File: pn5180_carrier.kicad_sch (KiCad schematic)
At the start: 35 parts, among them J1 Bay 0 (CLIK-Mate 1x10), J10 24V IN (CLIK-Mate 1x2), J2 Bay 1 (CLIK-Mate 1x10), J3 Bay 2 (CLIK-Mate 1x10), J4 Bay 3 (CLIK-Mate 1x10), J5 Bay 4 (CLIK-Mate 1x10), J6 Bay 5 (CLIK-Mate 1x10), J7 Bay 6 (CLIK-Mate 1x10), J8 Bay 7 (CLIK-Mate 1x10), U1 74HC138, U2 74HC151, U4 TLV1117LV33DCYR, U5 XIAO ESP32C6, U6 MP1584EN module (set 5.0V)

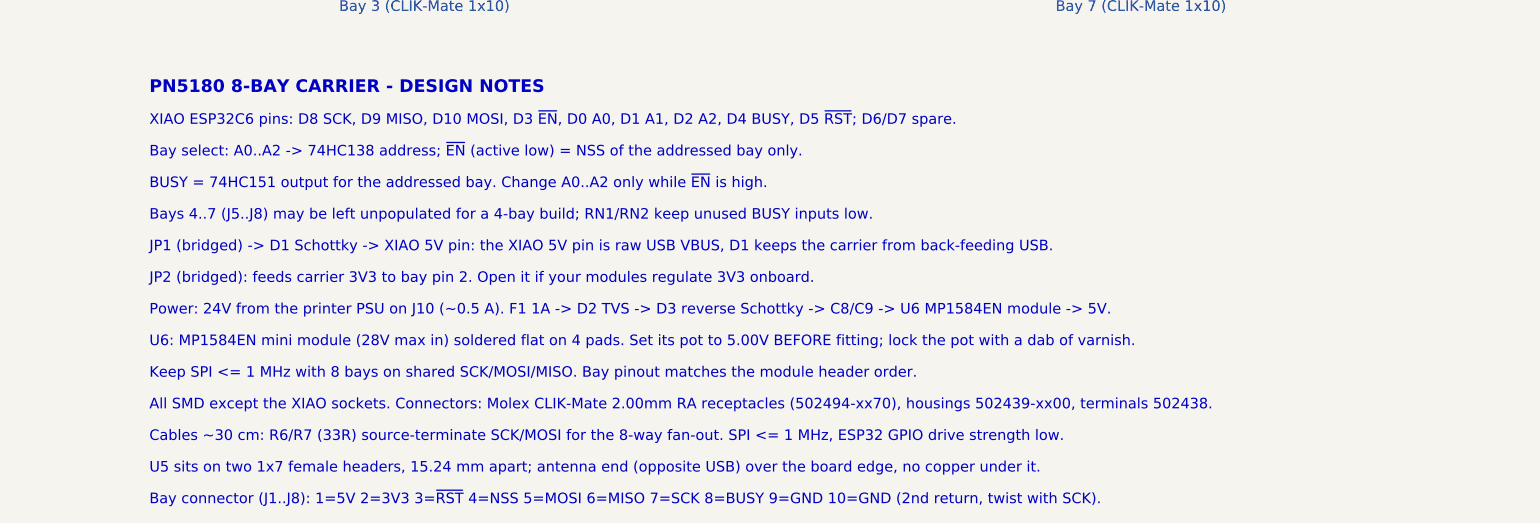
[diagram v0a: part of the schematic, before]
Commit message: Schematic notes: drop JP1/JP2 wording; re-export the PDF/PNG renders
Two DESIGN NOTES text objects only; netlist (38 nets, 189 nodes, 0 problems)
and ERC (1 error, 81 warnings) unchanged.

Co-Authored-By: Claude Fable 5.1 <noreply@anthropic.com>
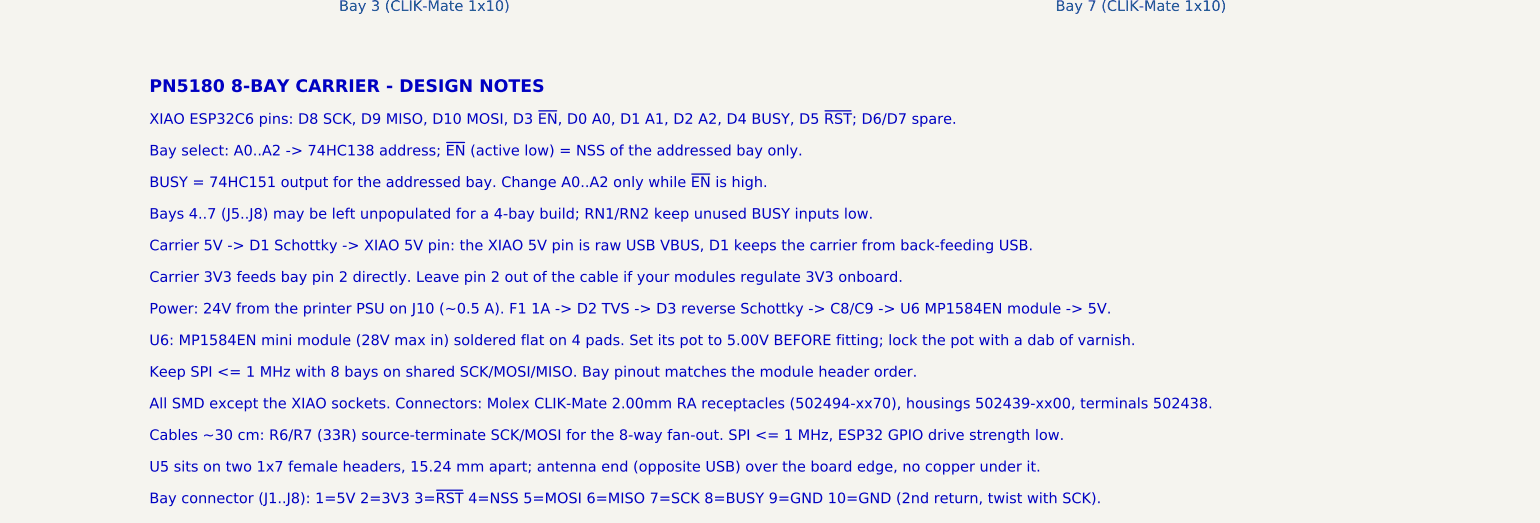
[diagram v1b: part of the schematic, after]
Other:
- note added: "Carrier 3V3 feeds bay pin 2 directly. Leave pin 2 out of the cable if your modules regulate 3V3 onboard."
- note added: "Carrier 5V -> D1 Schottky -> XIAO 5V pin: the XIAO 5V pin is raw USB VBUS, D1 keeps the carrier from back-feeding USB."
- note removed: "JP1 (bridged) -> D1 Schottky -> XIAO 5V pin: the XIAO 5V pin is raw USB VBUS, D1 keeps the carrier from back-feeding USB."
- note removed: "JP2 (bridged): feeds carrier 3V3 to bay pin 2. Open it if your modules regulate 3V3 onboard."
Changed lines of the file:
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@@
 		)
 	)
-	(text "JP1 (bridged) -> D1 Schottky -> XIAO 5V pin: the XIAO 5V pin is raw USB VBUS, D1 keeps the carrier from back-feeding USB."
+	(text "Carrier 5V -> D1 Schottky -> XIAO 5V pin: the XIAO 5V pin is raw USB VBUS, D1 keeps the carrier from back-feeding USB."
 		(exclude_from_sim no)
 		(at 243.84 207.01 0)
@@
 		)
 	)
-	(text "JP2 (bridged): feeds carrier 3V3 to bay pin 2. Open it if your modules regulate 3V3 onboard."
+	(text "Carrier 3V3 feeds bay pin 2 directly. Leave pin 2 out of the cable if your modules regulate 3V3 onboard."
 		(exclude_from_sim no)
 		(at 243.84 210.82 0)
